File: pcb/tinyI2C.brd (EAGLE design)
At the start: 100 x 84.4 mm, 39 parts, among them IC1 74LVC1G125DCK, IC2 74LVC1G125DCK, IC3 IC_LDO_MIC5355, Q1 12MHz, U1 LPC824M201JHI33, X1 TSW-112-02-S-S, X2 TSW-112-02-S-S, X3 TSW-106-02-S-S-RA, X4 TSW-102-02-S-S, X5 TSW-102-02-S-S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

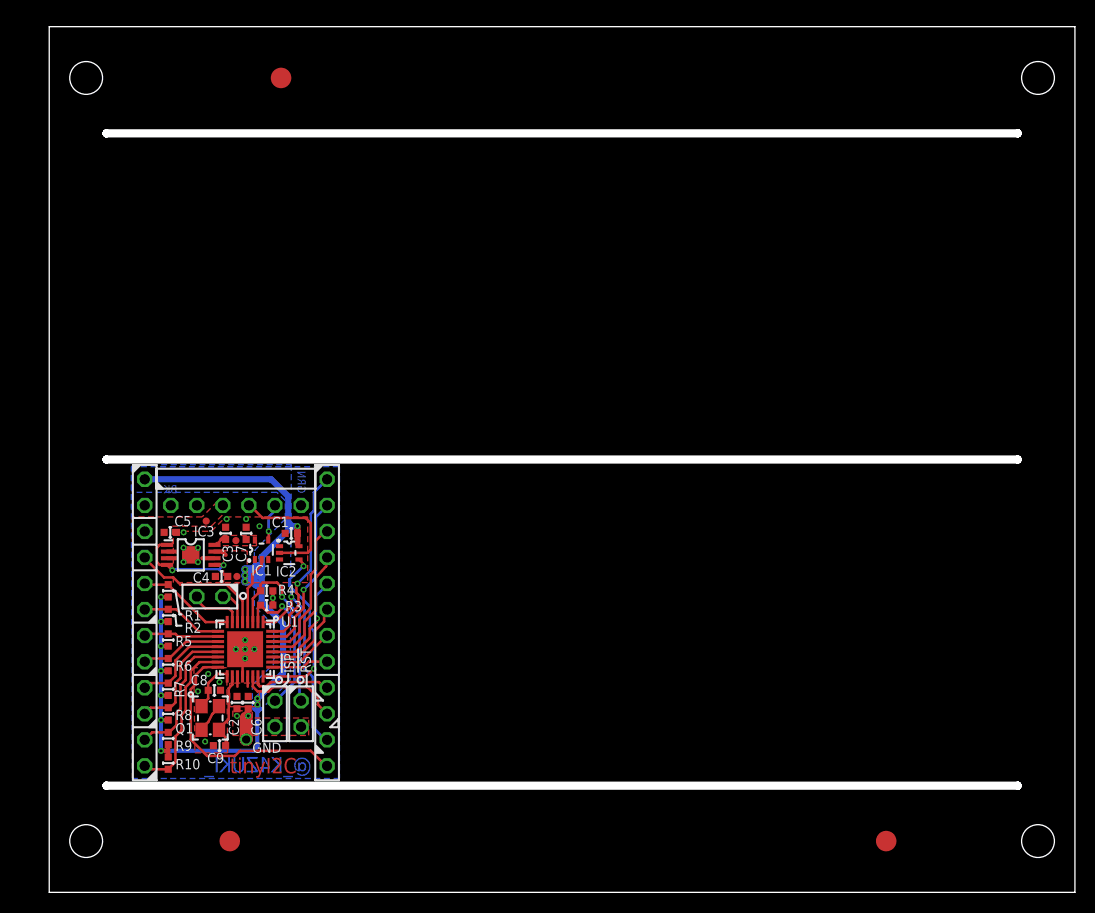
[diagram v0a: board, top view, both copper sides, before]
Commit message: [ PCB ] panel/drill size change, V-CUT mark, Panelize
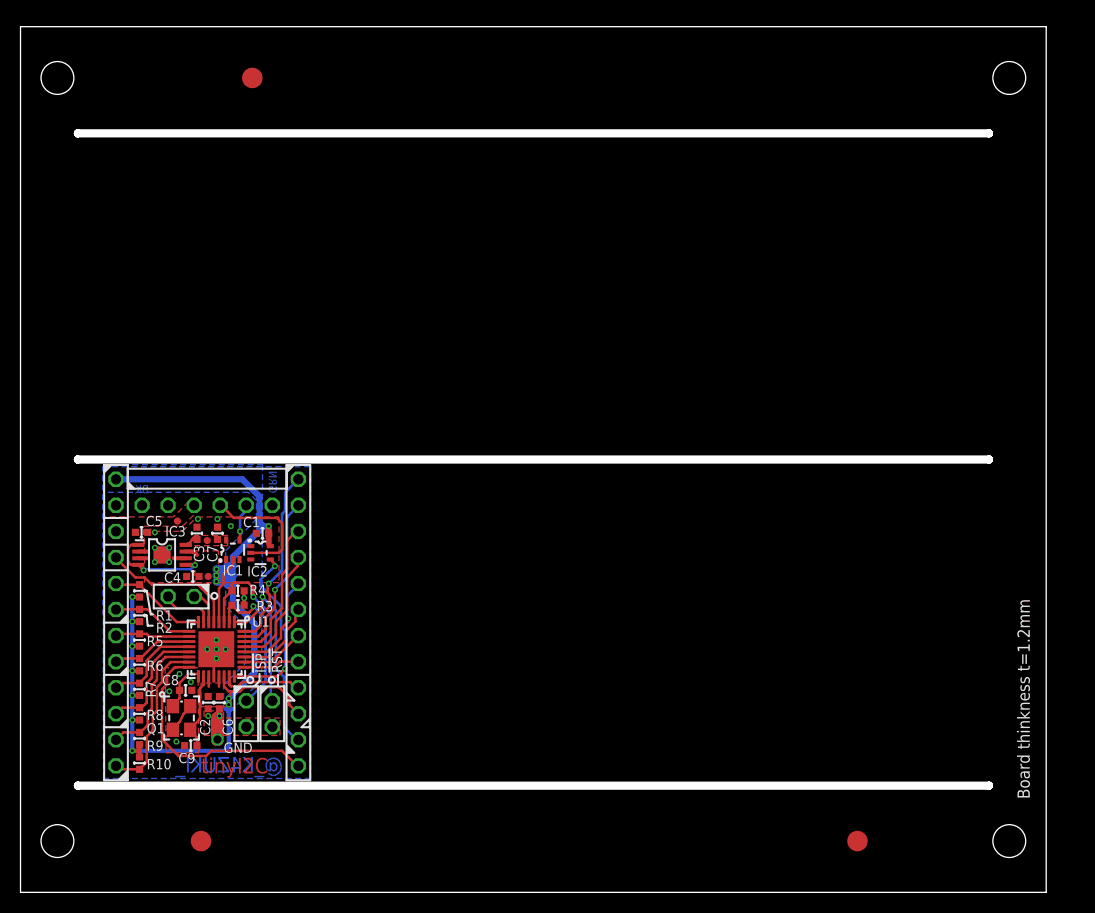
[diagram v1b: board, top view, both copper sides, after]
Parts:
- moved TP5 2.80 mm to (81.6, 5.00)
- moved C2 2.80 mm to (18.3, 18.5)
- moved C3 2.80 mm to (17.2, 35.0)
- moved C4 2.80 mm to (16.8, 30.8)
- moved C6 2.80 mm to (19.4, 18.5)
- moved C7 2.80 mm to (19.2, 35.0)
- moved I1 2.80 mm to (17.2, 22.5)
- moved IC1 2.80 mm to (20.7, 33.4)
- moved IC2 2.80 mm to (23.4, 33.1)
- moved IC3 2.80 mm to (13.8, 32.9)
- moved Q1 2.80 mm to (15.7, 17.0)
- moved R1 2.80 mm to (11.6, 29.4)
- moved R10 2.80 mm to (11.6, 12.6)
- moved R2 2.80 mm to (11.6, 27.0)
- moved R3 2.80 mm to (21.2, 28.0)
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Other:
- board text added: "Board thinkness t=1.2mm"

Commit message: [ FIX ] horizontal milling width increased to 1.0mm
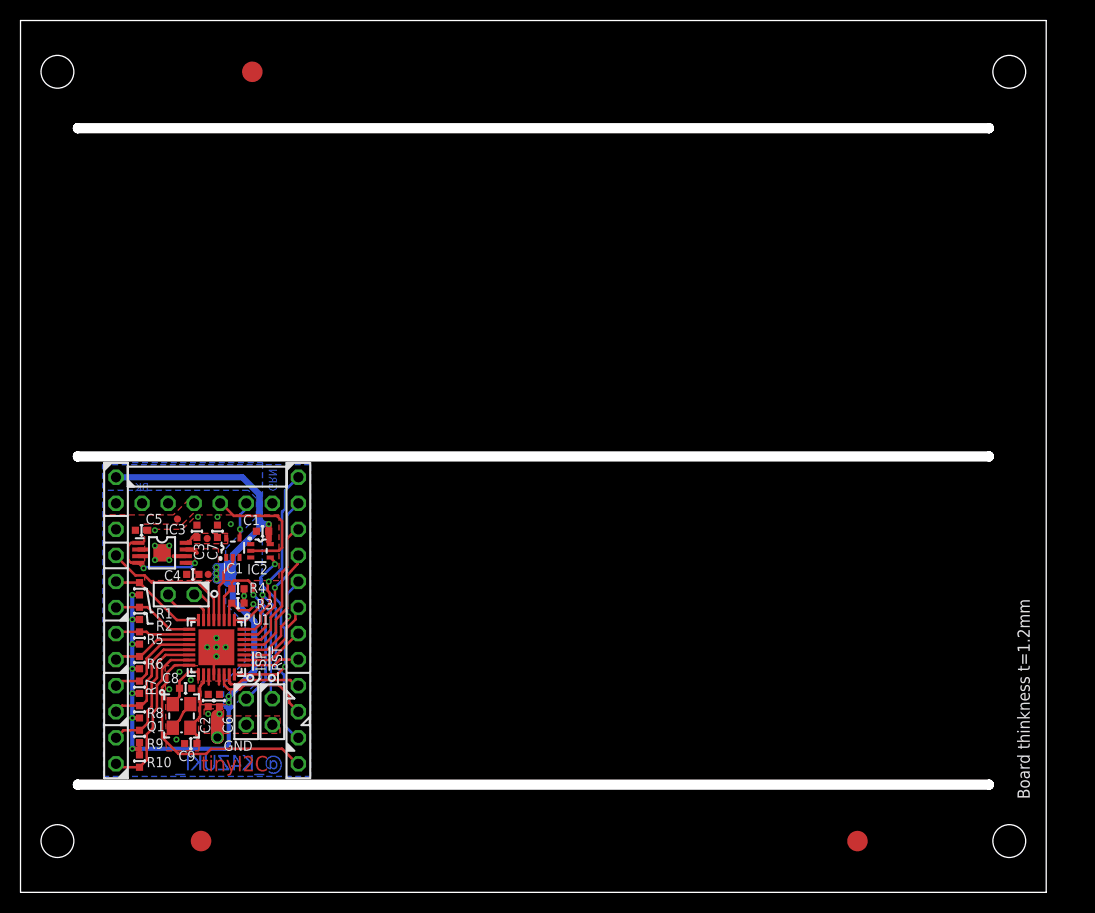
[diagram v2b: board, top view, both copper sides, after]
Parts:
- moved TP4 0.60 mm to (22.6, 80.0)
- moved C1 0.20 mm to (23.6, 35.2)
- moved C3 0.20 mm to (17.2, 35.2)
- moved C7 0.20 mm to (19.2, 35.2)
- moved IC1 0.20 mm to (20.7, 33.6)
- moved IC3 0.20 mm to (13.8, 33.1)
- moved R1 0.20 mm to (11.6, 29.6)
- moved R4 0.20 mm to (21.2, 29.6)
- moved R8 0.20 mm to (11.6, 17.6)
- moved TP6 0.20 mm to (18.2, 34.5)
- moved X3 0.20 mm to (18.2, 39.5)
- moved R10 0.20 mm to (11.6, 12.8)
- moved C2 0.20 mm to (18.3, 18.7)
- moved C4 0.20 mm to (16.8, 31.0)
- moved C6 0.20 mm to (19.4, 18.7)
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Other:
- board size 100 x 84.4 mm -> 100 x 85 mm

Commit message: .
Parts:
- removed TP6: TPTP07R, testpad_local:TP07R
- TP2: value TPTP07R -> TESTPAD; device testpad_local:TP07R -> mylib:TP06RECT
- moved C3 0.40 mm to (17.6, 35.2)
- moved TP2 0.10 mm to (18.4, 31.0)
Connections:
- net 3.3V: no longer TP6.TP
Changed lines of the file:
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@@
 <wire x1="23.4" y1="35.6" x2="22.6" y2="35.6" width="0.1" layer="41"/>
 <wire x1="18.8" y1="35.4" x2="18.8" y2="36.1" width="0.1" layer="41"/>
-<wire x1="17.6" y1="35.4" x2="17.6" y2="36.1" width="0.1" layer="41"/>
-<wire x1="16.8" y1="35.4" x2="16.8" y2="35.6" width="0.1" layer="41"/>
+<wire x1="18" y1="35.4" x2="18" y2="36.1" width="0.1" layer="41"/>
+<wire x1="17.2" y1="35.4" x2="17.2" y2="35.6" width="0.1" layer="41"/>
 <wire x1="11.6" y1="35.7" x2="10.9" y2="35.7" width="0.1" layer="41"/>
 <wire x1="11.6" y1="34.9" x2="10.9" y2="34.9" width="0.1" layer="41"/>
 <wire x1="11.6" y1="34.9" x2="11.6" y2="35.7" width="0.1" layer="41"/>
-<wire x1="17.6" y1="35.4" x2="16.8" y2="35.4" width="0.1" layer="41"/>
+<wire x1="18" y1="35.4" x2="17.2" y2="35.4" width="0.1" layer="41"/>
 <wire x1="19.6" y1="35.4" x2="18.8" y2="35.4" width="0.1" layer="41"/>
 <rectangle x1="15.6" y1="5" x2="17.6" y2="7" layer="29"/>
@@
 <attribute name="VALUE" x="15.046" y="35.892" size="0.0254" layer="27"/>
 </element>
-<element name="TP2" library="testpad_local" package="TP07R" value="TPTP07R" x="18.3" y="31" smashed="yes">
-<attribute name="TP_SIGNAL_NAME" value="" x="18.3" y="29.095" size="1" layer="37"/>
-<attribute name="VALUE" x="18.046" y="30.492" size="0.0254" layer="27"/>
-</element>
 <element name="TP3" library="testpad_local" package="B1,27" value="TPB1,27" x="19.2" y="15.1" smashed="yes">
 <attribute name="TP_SIGNAL_NAME" value="" x="19.2" y="13.195" size="1" layer="37"/>
@@
 <attribute name="VALUE" x="13.505" y="12.165" size="1.27" layer="27" rot="R90"/>
 </element>
-<element name="C3" library="mylib" package="C0402" value="10u/1005" x="17.2" y="35.2" smashed="yes" rot="R90">
-<attribute name="NAME" x="17.9" y="32.4" size="1" layer="25" font="vector" ratio="20" rot="R90"/>
-<attribute name="VALUE" x="19.105" y="34.565" size="1.27" layer="27" rot="R90"/>
+<element name="C3" library="mylib" package="C0402" value="10u/1005" x="17.6" y="35.2" smashed="yes" rot="R90">
+<attribute name="NAME" x="18.1" y="32.4" size="1" layer="25" font="vector" ratio="20" rot="R90"/>
+<attribute name="VALUE" x="19.505" y="34.565" size="1.27" layer="27" rot="R90"/>
 </element>
 <element name="X1" library="con-samtec.local" package="TSW-112-02-S-S" value="TSW-112-02-S-S" x="9.31" y="26.5" smashed="yes" rot="R90">
@@
 <attribute name="VALUE" x="23.28" y="22.055" size="1.27" layer="27" rot="R180"/>
 </element>
-<element name="TP6" library="testpad_local" package="TP07R" value="TPTP07R" x="18.2" y="34.5" smashed="yes">
-<attribute name="TP_SIGNAL_NAME" value="" x="18.2" y="32.595" size="1" layer="37"/>
-<attribute name="VALUE" x="17.946" y="33.992" size="0.0254" layer="27"/>
-</element>
 <element name="IC1" library="74xx-little-us_local" package="SC70-5" value="74LVC1G125DCK" x="20.7" y="33.6" smashed="yes">
 <attribute name="NAME" x="19.7" y="31.1" size="1" layer="25" font="vector" ratio="20"/>
@@
 </element>
 <element name="I1" library="mylib" package="ICON_MINLAB_5.2MM" value="ICON_MINLAB_5.2S" x="17.2" y="22.7" rot="MR0"/>
+<element name="TP2" library="mylib" package="TP06RECT" value="TESTPAD" x="18.4" y="31" smashed="yes">
+<attribute name="VALUE" x="18.146" y="30.619" size="0.0254" layer="27"/>
+</element>
 </elements>
 <signals>
@@
 <wire x1="14.85" y1="16.25" x2="15.5" y2="16.8" width="0.25" layer="1"/>
 <via x="13.1" y="35.3" extent="1-16" drill="0.3"/>
-<via x="17.3" y="36.6" extent="1-16" drill="0.3"/>
+<via x="17.6" y="36.6" extent="1-16" drill="0.3"/>
 <via x="19.2" y="36.6" extent="1-16" drill="0.3"/>
 <polygon width="0.25" layer="1" thermals="no" rank="2">
@@
 <contactref element="C4" pad="1"/>
 <contactref element="C2" pad="1"/>
-<contactref element="TP2" pad="TP"/>
 <contactref element="R1" pad="2"/>
 <contactref element="R2" pad="2"/>
@@
 <wire x1="10.9" y1="14" x2="19.9" y2="14" width="0.4" layer="16"/>
 <wire x1="19.9" y1="14" x2="20.3" y2="14.4" width="0.4" layer="16"/>
-<wire x1="16.112" y1="33.426" x2="16.874" y2="33.426" width="0.4" layer="1"/>
-<wire x1="16.874" y1="33.426" x2="17.2" y2="33.1" width="0.4" layer="1"/>
+<wire x1="16.112" y1="33.426" x2="17.074" y2="33.426" width="0.4" layer="1"/>
+<wire x1="17.074" y1="33.426" x2="17.4" y2="33.1" width="0.4" layer="1"/>
 <contactref element="IC2" pad="5"/>
 <polygon width="0.25" layer="1" thermals="no">
@@
 <wire x1="24.2" y1="35.9" x2="23.7" y2="35.9" width="0.6" layer="16"/>
 <wire x1="23.7" y1="35.9" x2="23.3" y2="35.5" width="0.6" layer="16"/>
+<contactref element="TP2" pad="TP"/>
 </signal>
 <signal name="TGT_TX">
@@
 <signal name="3.3V">
 <contactref element="C3" pad="1"/>
-<contactref element="TP6" pad="TP"/>
 <wire x1="16.112" y1="34.076" x2="16.276" y2="34.076" width="0.25" layer="1"/>
 <wire x1="16.276" y1="34.076" x2="16.9" y2="34.7" width="0.25" layer="1"/>

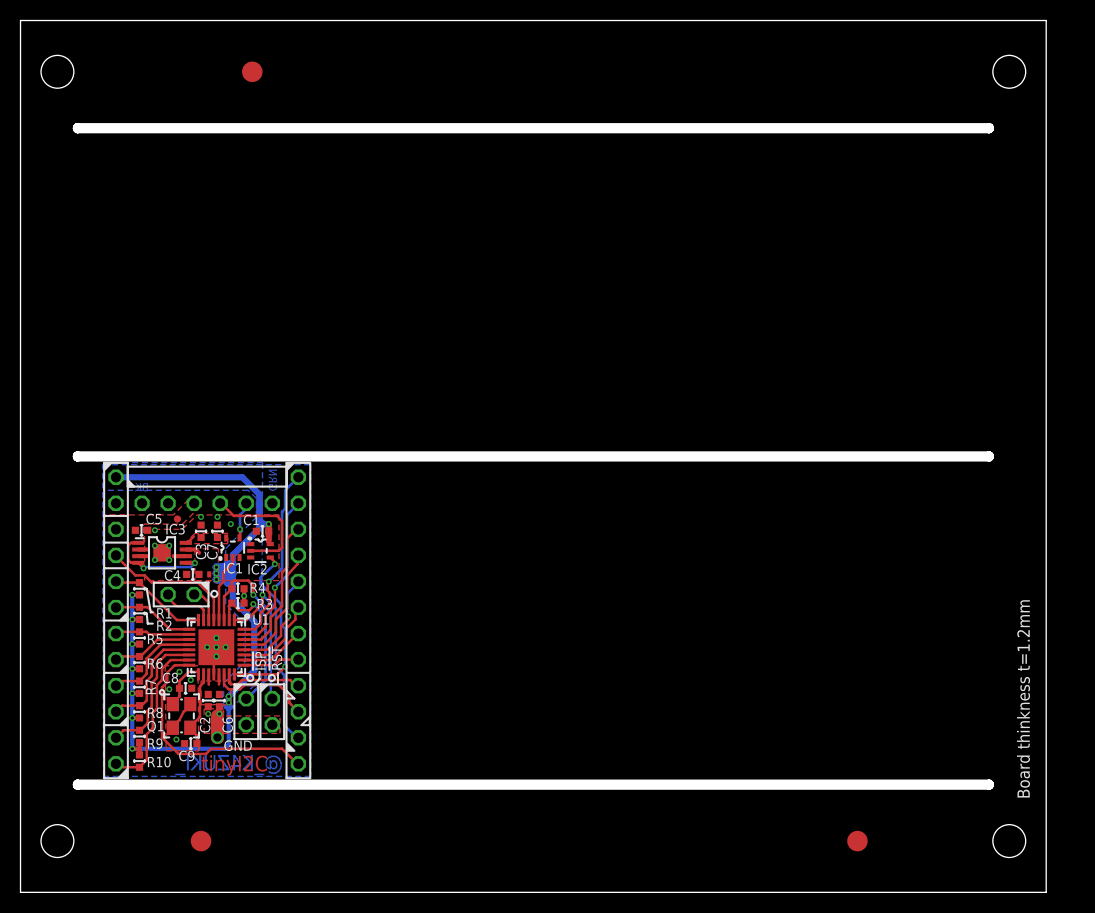
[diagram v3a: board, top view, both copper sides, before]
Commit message: [ PCB ][ SCH ] FIDUCIAL from library
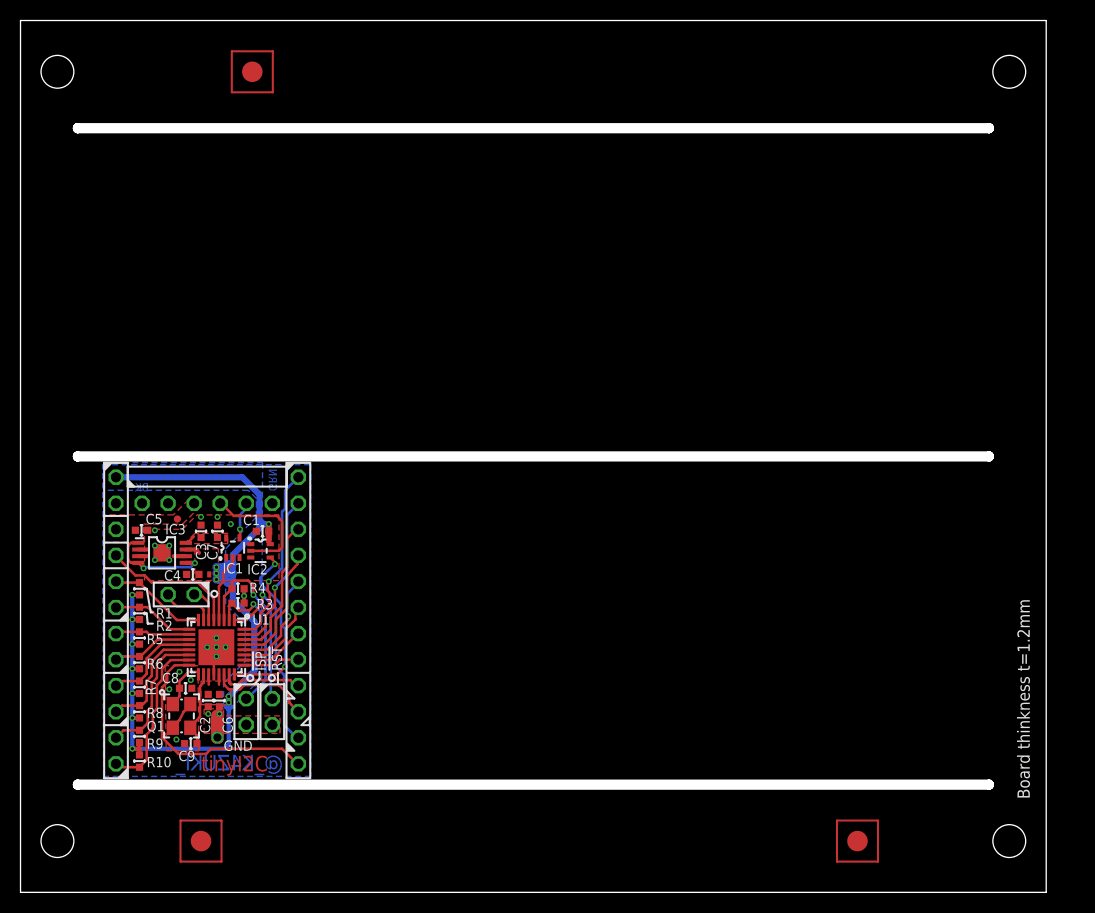
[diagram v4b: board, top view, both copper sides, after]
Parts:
- TP4, TP5, TP8: value TPTP20R -> TESTPAD_F; device testpad_local:TP20R -> mylib:FIDUCIAL
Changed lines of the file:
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@@
 <dimension x1="50.4" y1="0" x2="70.8" y2="0" x3="60.6" y3="-4" textsize="1.27" textratio="10" layer="47" visible="yes"/>
 <dimension x1="71.6" y1="0" x2="92" y2="0" x3="81.8" y3="-4" textsize="1.27" textratio="10" layer="47" visible="yes"/>
-<rectangle x1="20.6" y1="80" x2="22.6" y2="82" layer="29"/>
-<rectangle x1="79.6" y1="5" x2="81.6" y2="7" layer="29"/>
 <wire x1="8.2" y1="41.6" x2="28.2" y2="41.6" width="0.4" layer="42"/>
 <wire x1="8.2" y1="11" x2="8.2" y2="41.6" width="0.4" layer="42"/>
@@
 <wire x1="18" y1="35.4" x2="17.2" y2="35.4" width="0.1" layer="41"/>
 <wire x1="19.6" y1="35.4" x2="18.8" y2="35.4" width="0.1" layer="41"/>
-<rectangle x1="15.6" y1="5" x2="17.6" y2="7" layer="29"/>
 <wire x1="0" y1="85" x2="0" y2="0" width="0" layer="20"/>
 <wire x1="100" y1="85" x2="100" y2="0" width="0" layer="20"/>
@@
 <vertex x="5.35" y="10.5" curve="-90"/>
 </polygon>
-<rectangle x1="17.6" y1="5" x2="19.6" y2="7" layer="29"/>
-<rectangle x1="15.6" y1="3" x2="17.6" y2="5" layer="29"/>
-<rectangle x1="17.6" y1="3" x2="19.6" y2="5" layer="29"/>
-<rectangle x1="22.6" y1="80" x2="24.6" y2="82" layer="29"/>
-<rectangle x1="22.6" y1="78" x2="24.6" y2="80" layer="29"/>
-<rectangle x1="20.6" y1="78" x2="22.6" y2="80" layer="29"/>
-<rectangle x1="81.6" y1="5" x2="83.6" y2="7" layer="29"/>
-<rectangle x1="81.6" y1="3" x2="83.6" y2="5" layer="29"/>
-<rectangle x1="79.6" y1="3" x2="81.6" y2="5" layer="29"/>
 <dimension x1="50.4" y1="0" x2="70.8" y2="0" x3="60.6" y3="-4" textsize="1.27" textratio="10" layer="47" visible="yes"/>
 <wire x1="7.6" y1="-0.5" x2="7.2" y2="-0.9" width="0.2" layer="102"/>
@@
 <attribute name="VALUE" x="25.82" y="22.055" size="1.27" layer="27" rot="R180"/>
 </element>
-<element name="TP4" library="testpad_local" package="TP20R" value="TPTP20R" x="22.6" y="80" smashed="yes">
-<attribute name="TP_SIGNAL_NAME" value="" x="22.6" y="78.095" size="1" layer="37"/>
+<element name="TP4" library="mylib" package="FIDUCIAL" value="TESTPAD_F" x="22.6" y="80" smashed="yes">
 <attribute name="VALUE" x="22.346" y="79.492" size="0.0254" layer="27"/>
 </element>
-<element name="TP5" library="testpad_local" package="TP20R" value="TPTP20R" x="81.6" y="5" smashed="yes">
-<attribute name="TP_SIGNAL_NAME" value="" x="81.6" y="3.095" size="1" layer="37"/>
+<element name="TP5" library="mylib" package="FIDUCIAL" value="TESTPAD_F" x="81.6" y="5" smashed="yes">
 <attribute name="VALUE" x="81.346" y="4.492" size="0.0254" layer="27"/>
 </element>
@@
 <attribute name="VALUE" x="19.835" y="14.338" size="0.0254" layer="28" rot="MR0"/>
 </element>
-<element name="TP8" library="testpad_local" package="TP20R" value="TPTP20R" x="17.6" y="5" smashed="yes">
-<attribute name="TP_SIGNAL_NAME" value="" x="17.6" y="3.095" size="1" layer="37"/>
+<element name="TP8" library="mylib" package="FIDUCIAL" value="TESTPAD_F" x="17.6" y="5" smashed="yes">
 <attribute name="VALUE" x="17.219" y="4.492" size="0.0254" layer="27"/>
 </element>
